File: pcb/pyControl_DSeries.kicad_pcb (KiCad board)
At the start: 2 copper layers, 90.2 x 66.5 mm, 17 parts, among them J1 USB_micro_horz_socket_reinfor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, J2 RJ45-12PORT, J3 Barrel_Jack, U1 PyBoard-D-Series, U2 R-78E5.0-1.0, U3 TBD62083APG, U4 TBD62083APG, U5 TBD62083APG, X1U1 Hirose_40_pin_connector, X2U1 Hirose_40_pin_connector

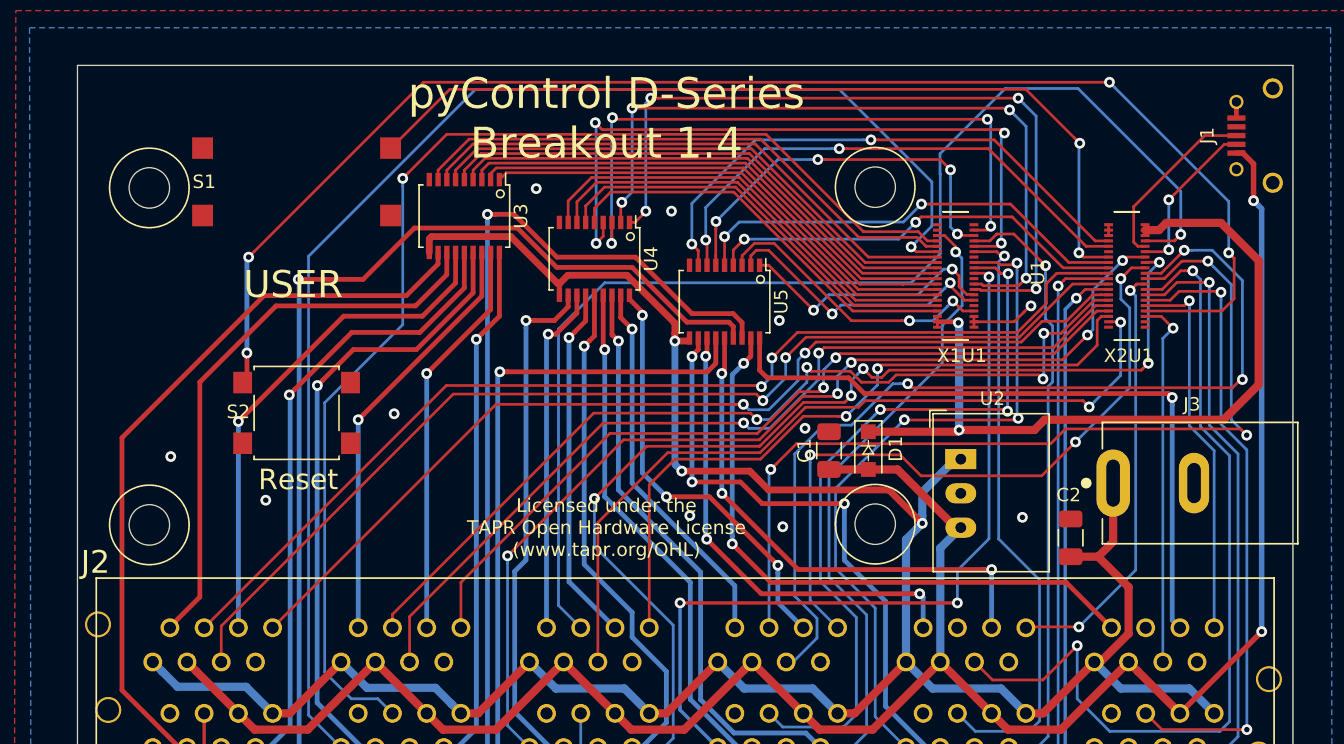
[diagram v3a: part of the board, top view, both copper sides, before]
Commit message: pcb v1.5. Rearranged pins to jack mapping.
To get top row inputs on separate interrupt vectors
T3_C was W74, now Q24
T4_B was W62, now W68
T4_C was W60, now W66
T6_A was W50, now W65
T6_A was W46, now W71

To maximize the number of analog inputs that are exposed
T4_A was W64, now W10
B3_A is now W63
B3_B is now W14

Design constraint priorities
All ports must have power 2 power pins and at least 2 DIO
DACs are grouped with I2c peripherals
All of peripherals are on bottom row
All if IO pins on top row are on separate external interrupt vectors. If you use the top ports for your digital inputs, you will never risk having conflicts of having already used an interrupt vector
15 Analog input pins are distributed through the DIO pins
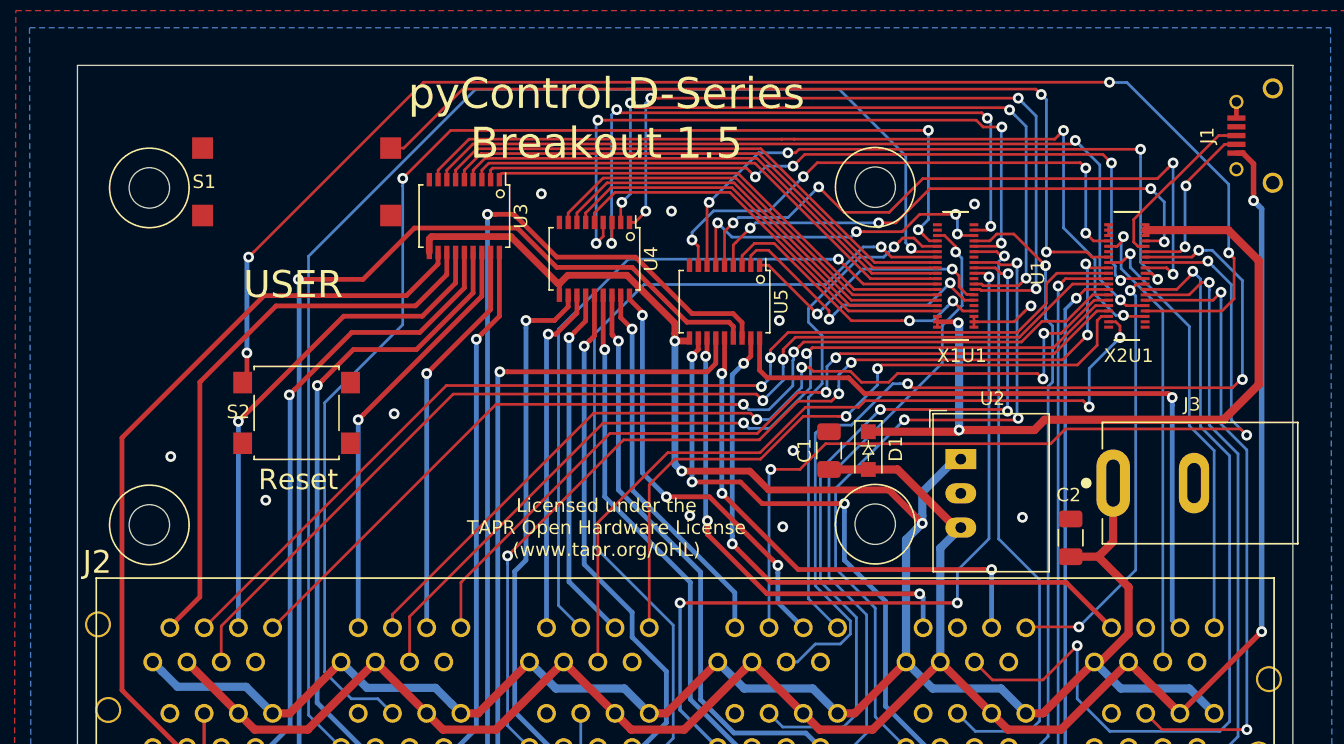
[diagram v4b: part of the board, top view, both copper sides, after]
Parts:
- D1: value Diode -> Schottky Diode
- J1: value USB_micro_horz_socket_reinforced -> MicroUSB Connector
- J2: value RJ45-12PORT -> 12-port RJ45
- J3: value Barrel_Jack -> Barrel Jack
- S1: value TL3300 -> Large Tactile Switch
- S2: value B3FS-1010P -> Small Tactile Switch
- U1: value PyBoard-D-Series -> pyboard-D-series
- U2: value R-78E5.0-1.0 -> Voltage Regulator
- U3, U4, U5: value TBD62083APG -> TBD62083A
- X1U1, X2U1: value Hirose_40_pin_connector -> 40-pin Connector
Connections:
- U1 pad 10: /B1_COMA -> /T4_DA
- U1 pad 14: /T1_COMB -> /B3_DB
- U1 pad 24: /T2_COMA -> /T3_DC
- U1 pad 46: /T6_DB -> /B1_COMA
- U1 pad 50: /T6_DA -> /T1_COMB
- U1 pad 60: /T4_DC -> /T2_COMA
- U1 pad 62: /T4_DB -> /T5_COMB
- U1 pad 63: /B6_COMA -> /B3_DA
- U1 pad 64: /T4_DA -> /T5_COMA
- U1 pad 65: /T5_COMA -> /T6_DA
- U1 pad 66: /B3_DB -> /T4_DC
- U1 pad 68: /B3_DA -> /T4_DB
- U1 pad 71: /T5_COMB -> /T6_DB
- U1 pad 74: /T3_DC -> /B6_COMA
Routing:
- net /T3_DC: track 90.0 -> 53.9 mm
- net /B1_COMA: track 42.0 -> 65.9 mm, vias 0 -> 2
- net /T1_COMB: track 41.4 -> 63.5 mm, vias 0 -> 2
- net /T2_COMA: track 37.3 -> 58.9 mm, vias 0 -> 4
- net /T5_COMA: track 33.4 -> 50.0 mm, vias 2 -> 4
- net /B3_DB: track 86.6 -> 71.9 mm, vias 5 -> 1
- net /T4_DA: track 51.2 -> 37.4 mm, vias 3 -> 1
- net /T5_COMB: track 39.0 -> 49.7 mm, vias 2 -> 4
- net /B6_COMA: track 31.6 -> 40.0 mm, vias 2 -> 4
- net /T6_DB: track 27.5 -> 34.5 mm
- net /B2_DB: track 89.6 -> 95.2 mm, vias 1 -> 3
- net /B5_COMB: track 29.1 -> 24.8 mm
- net /T6_DA: track 28.4 -> 32.2 mm
- net /USR: track 65.1 -> 66.9 mm
- net /T4_DB: track 69.3 -> 70.9 mm
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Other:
- board text added: "pyControl D-Series Breakout 1.5"
- board text removed: "pyControl D-Series Breakout 1.4"

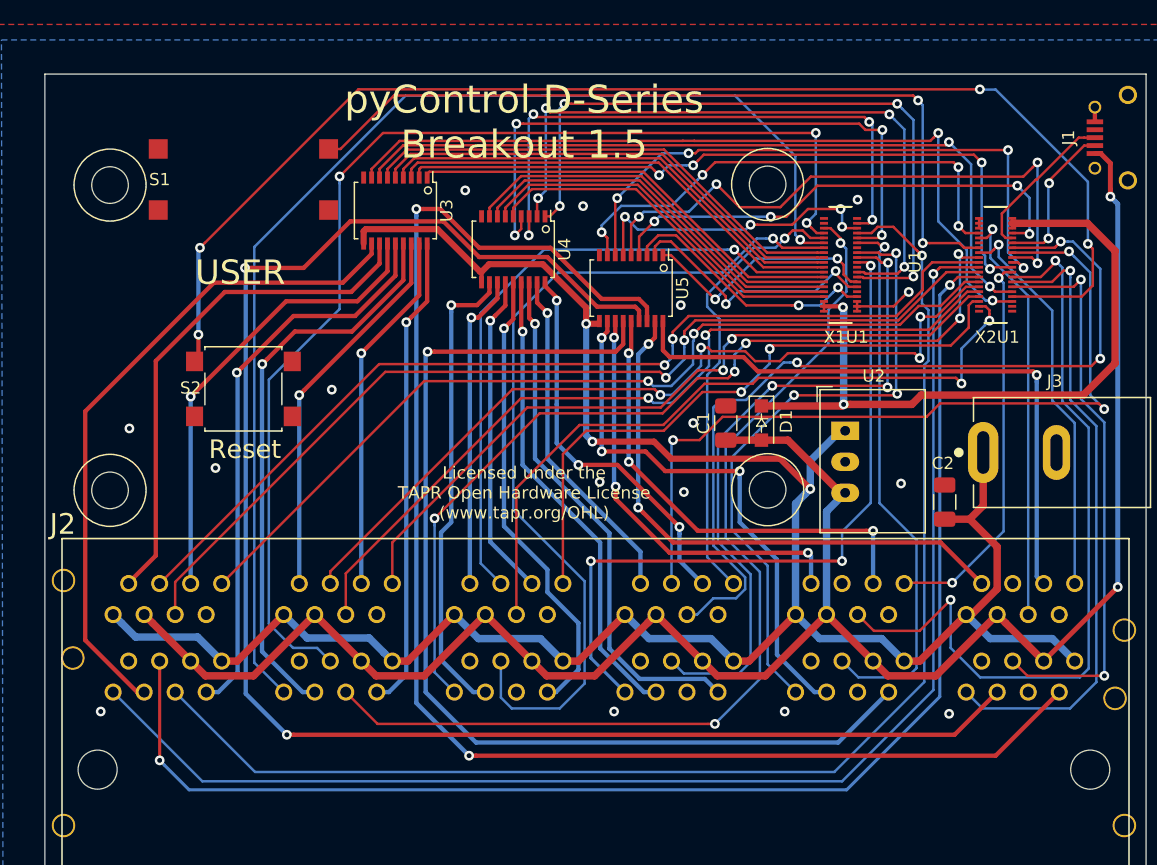
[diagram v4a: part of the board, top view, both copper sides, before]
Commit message: pcb v1.6. new rj45 footprint. swapped W49 and W51 so now interrupt vector 13 is on DIO_C of port 2. can have entire row of DIO-A and DIO-B interrupts without collisions
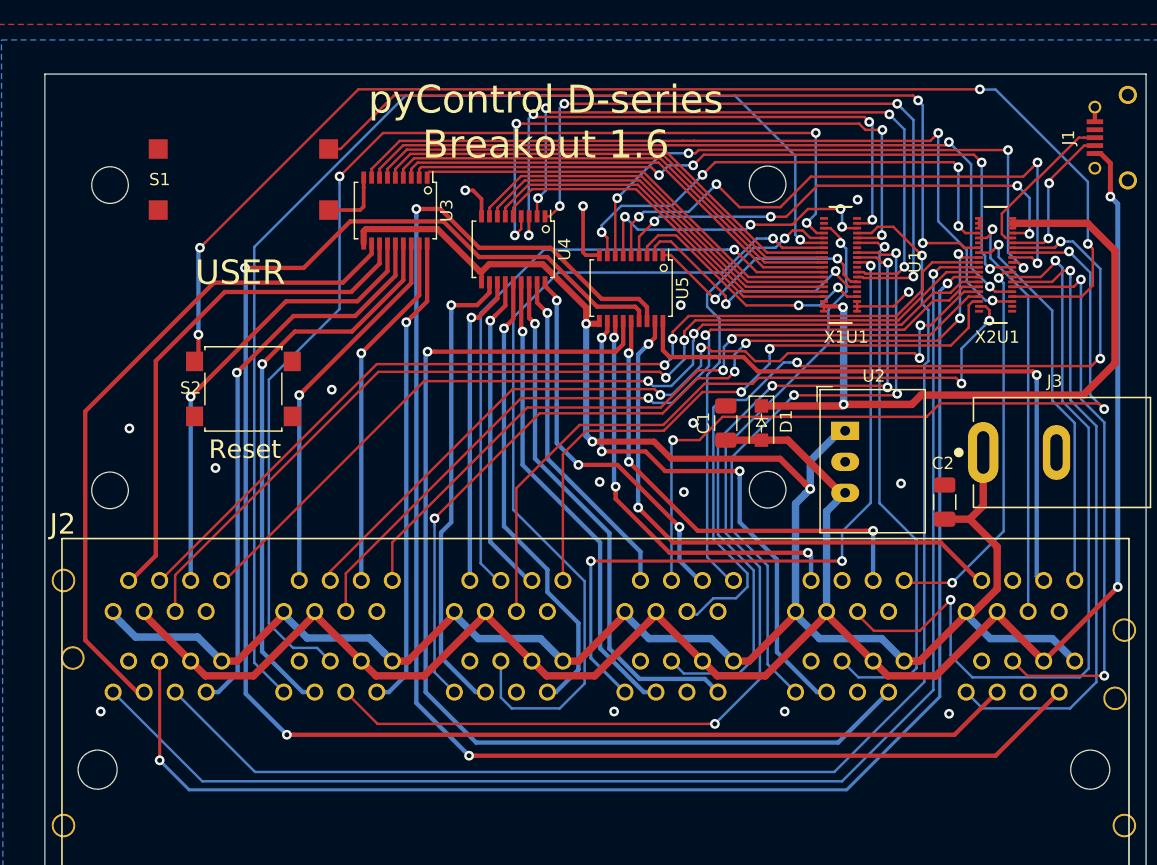
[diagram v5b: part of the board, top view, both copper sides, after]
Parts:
- D1: value Schottky Diode -> MBR120VLSFT3G
- J1: value MicroUSB Connector -> 10118194-0001LF
- J2: value 12-port RJ45 -> 5569263-1
- J3: value Barrel Jack -> PJ-037A
- S1: value Large Tactile Switch -> TL3300DF160Q
- S2: value Small Tactile Switch -> B3FS-1010P
- U2: value Voltage Regulator -> R-78E5.0-1.0
- X1U1, X2U1: value 40-pin Connector -> DF40HC(4.0)-40DS-0.4V(70)
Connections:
- U1 pad 49: /T2_DB -> /T2_DC
- U1 pad 51: /T2_DC -> /T2_DB
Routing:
- net /GND: track 8.49 -> 22.1 mm
- net /T2_DC: track 68.2 -> 67.7 mm
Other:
- board text added: "pyControl D-series Breakout 1.6"
- board text removed: "Licensed under the TAPR Open Hardware License (www.tapr.org/OHL)"
- board text removed: "pyControl D-Series Breakout 1.5"

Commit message: update PCB files to KiCad v6
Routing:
- net /GND: track 22.1 -> 22.8 mm
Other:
- net class Default removed
- net class POWER removed
